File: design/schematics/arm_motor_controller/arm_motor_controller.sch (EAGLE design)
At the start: 59 parts, among them Q1 PFET-FQP27P06, Q2 PFET-FQP27P06, Q3 NFET-FQP30N06L, Q4 NFET-FQP30N06L, Q5 PFET-FQP27P06, Q6 PFET-FQP27P06, Q7 NFET-FQP30N06L, Q8 NFET-FQP30N06L, U1 V_REG_LD1085D2

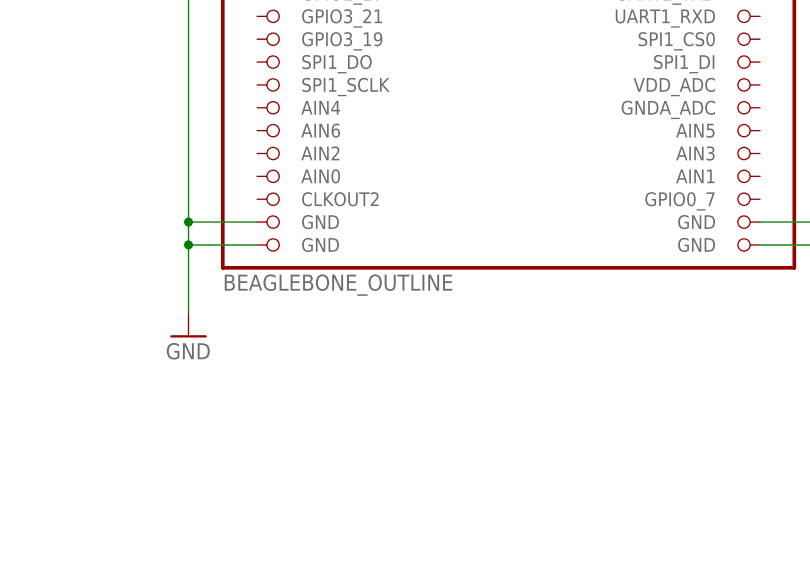
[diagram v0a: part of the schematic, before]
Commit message: updated adafruit library
to have a version of the board which only shows the outline, but doesn't
set the dimension layer.  also added the adafruit library to the repo
for use with other schematics.
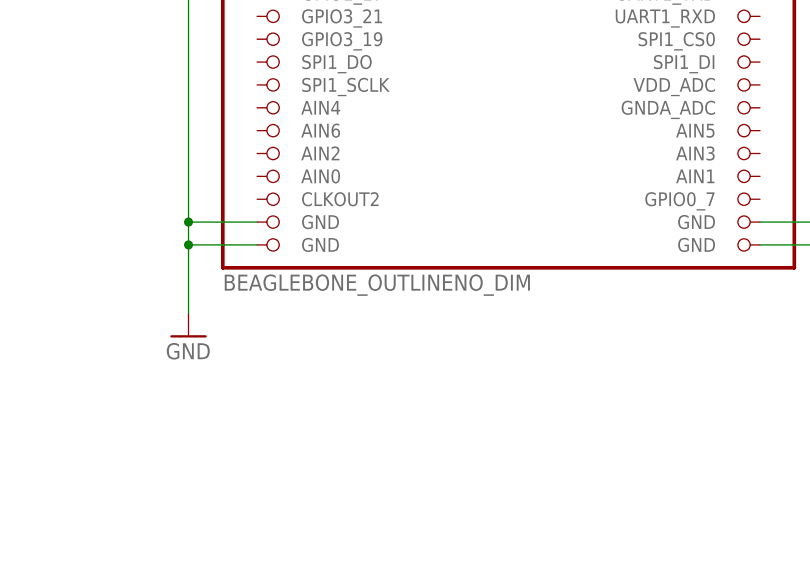
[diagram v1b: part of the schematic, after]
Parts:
- U$1: value BEAGLEBONE_OUTLINE -> BEAGLEBONE_OUTLINENO_DIM; device adafruit:BEAGLEBONE_OUTLINE -> adafruit:BEAGLEBONE_OUTLINENO_DIM
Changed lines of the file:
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@@
 <grid distance="0.1" unitdist="inch" unit="inch" style="lines" multiple="1" display="no" altdistance="0.01" altunitdist="inch" altunit="inch"/>
 <layers>
-<layer number="1" name="Top" color="4" fill="1" visible="no" active="no"/>
-<layer number="2" name="Route2" color="1" fill="3" visible="no" active="no"/>
-<layer number="3" name="Route3" color="4" fill="3" visible="no" active="no"/>
-<layer number="14" name="Route14" color="1" fill="6" visible="no" active="no"/>
-<layer number="15" name="Route15" color="4" fill="6" visible="no" active="no"/>
-<layer number="16" name="Bottom" color="1" fill="1" visible="no" active="no"/>
-<layer number="17" name="Pads" color="2" fill="1" visible="no" active="no"/>
-<layer number="18" name="Vias" color="2" fill="1" visible="no" active="no"/>
-<layer number="19" name="Unrouted" color="6" fill="1" visible="no" active="no"/>
-<layer number="20" name="Dimension" color="15" fill="1" visible="no" active="no"/>
-<layer number="21" name="tPlace" color="7" fill="1" visible="no" active="no"/>
-<layer number="22" name="bPlace" color="7" fill="1" visible="no" active="no"/>
-<layer number="23" name="tOrigins" color="15" fill="1" visible="no" active="no"/>
-<layer number="24" name="bOrigins" color="15" fill="1" visible="no" active="no"/>
-<layer number="25" name="tNames" color="7" fill="1" visible="no" active="no"/>
-<layer number="26" name="bNames" color="7" fill="1" visible="no" active="no"/>
-<layer number="27" name="tValues" color="7" fill="1" visible="no" active="no"/>
-<layer number="28" name="bValues" color="7" fill="1" visible="no" active="no"/>
+<layer number="1" name="Top" color="4" fill="1" visible="yes" active="no"/>
+<layer number="2" name="Route2" color="1" fill="3" visible="yes" active="no"/>
+<layer number="3" name="Route3" color="4" fill="3" visible="yes" active="no"/>
+<layer number="14" name="Route14" color="1" fill="6" visible="yes" active="no"/>
+<layer number="15" name="Route15" color="4" fill="6" visible="yes" active="no"/>
+<layer number="16" name="Bottom" color="1" fill="1" visible="yes" active="no"/>
+<layer number="17" name="Pads" color="2" fill="1" visible="yes" active="no"/>
+<layer number="18" name="Vias" color="2" fill="1" visible="yes" active="no"/>
+<layer number="19" name="Unrouted" color="6" fill="1" visible="yes" active="no"/>
+<layer number="20" name="Dimension" color="15" fill="1" visible="yes" active="no"/>
+<layer number="21" name="tPlace" color="7" fill="1" visible="yes" active="no"/>
+<layer number="22" name="bPlace" color="7" fill="1" visible="yes" active="no"/>
+<layer number="23" name="tOrigins" color="15" fill="1" visible="yes" active="no"/>
+<layer number="24" name="bOrigins" color="15" fill="1" visible="yes" active="no"/>
+<layer number="25" name="tNames" color="7" fill="1" visible="yes" active="no"/>
+<layer number="26" name="bNames" color="7" fill="1" visible="yes" active="no"/>
+<layer number="27" name="tValues" color="7" fill="1" visible="yes" active="no"/>
+<layer number="28" name="bValues" color="7" fill="1" visible="yes" active="no"/>
 <layer number="29" name="tStop" color="7" fill="3" visible="no" active="no"/>
 <layer number="30" name="bStop" color="7" fill="6" visible="no" active="no"/>
@@
 <layer number="35" name="tGlue" color="7" fill="4" visible="no" active="no"/>
 <layer number="36" name="bGlue" color="7" fill="5" visible="no" active="no"/>
-<layer number="37" name="tTest" color="7" fill="1" visible="no" active="no"/>
-<layer number="38" name="bTest" color="7" fill="1" visible="no" active="no"/>
+<layer number="37" name="tTest" color="7" fill="1" visible="yes" active="no"/>
+<layer number="38" name="bTest" color="7" fill="1" visible="yes" active="no"/>
 <layer number="39" name="tKeepout" color="4" fill="11" visible="no" active="no"/>
 <layer number="40" name="bKeepout" color="1" fill="11" visible="no" active="no"/>
@@
 <layer number="44" name="Drills" color="7" fill="1" visible="no" active="no"/>
 <layer number="45" name="Holes" color="7" fill="1" visible="no" active="no"/>
-<layer number="46" name="Milling" color="3" fill="1" visible="no" active="no"/>
-<layer number="47" name="Measures" color="7" fill="1" visible="no" active="no"/>
-<layer number="48" name="Document" color="7" fill="1" visible="no" active="no"/>
-<layer number="49" name="Reference" color="7" fill="1" visible="no" active="no"/>
-<layer number="50" name="dxf" color="7" fill="1" visible="no" active="no"/>
-<layer number="51" name="tDocu" color="7" fill="1" visible="no" active="no"/>
-<layer number="52" name="bDocu" color="7" fill="1" visible="no" active="no"/>
-<layer number="53" name="tGND_GNDA" color="7" fill="9" visible="no" active="no"/>
-<layer number="54" name="bGND_GNDA" color="1" fill="9" visible="no" active="no"/>
-<layer number="56" name="wert" color="7" fill="1" visible="no" active="no"/>
-<layer number="57" name="tCAD" color="7" fill="1" visible="no" active="no"/>
+<layer number="46" name="Milling" color="3" fill="1" visible="yes" active="no"/>
+<layer number="47" name="Measures" color="7" fill="1" visible="yes" active="no"/>
+<layer number="48" name="Document" color="7" fill="1" visible="yes" active="no"/>
+<layer number="49" name="Reference" color="7" fill="1" visible="yes" active="no"/>
+<layer number="50" name="dxf" color="7" fill="1" visible="yes" active="no"/>
+<layer number="51" name="tDocu" color="7" fill="1" visible="yes" active="no"/>
+<layer number="52" name="bDocu" color="7" fill="1" visible="yes" active="no"/>
+<layer number="53" name="tGND_GNDA" color="7" fill="9" visible="yes" active="no"/>
+<layer number="54" name="bGND_GNDA" color="1" fill="9" visible="yes" active="no"/>
+<layer number="56" name="wert" color="7" fill="1" visible="yes" active="no"/>
+<layer number="57" name="tCAD" color="7" fill="1" visible="yes" active="no"/>
+<layer number="59" name="tCarbon" color="7" fill="1" visible="yes" active="no"/>
+<layer number="60" name="bCarbon" color="7" fill="1" visible="yes" active="no"/>
 <layer number="90" name="Modules" color="5" fill="1" visible="yes" active="yes"/>
 <layer number="91" name="Nets" color="2" fill="1" visible="yes" active="yes"/>
@@
 <layer number="113" name="IDFDebug" color="4" fill="1" visible="yes" active="yes"/>
 <layer number="116" name="Patch_BOT" color="9" fill="4" visible="yes" active="yes"/>
+<layer number="118" name="Rect_Pads" color="7" fill="1" visible="no" active="no"/>
 <layer number="121" name="_tsilk" color="7" fill="1" visible="yes" active="yes"/>
 <layer number="122" name="_bsilk" color="7" fill="1" visible="yes" active="yes"/>
@@
 <layer number="127" name="_tValues" color="7" fill="1" visible="yes" active="yes"/>
 <layer number="128" name="_bValues" color="7" fill="1" visible="yes" active="yes"/>
+<layer number="129" name="Mask" color="7" fill="1" visible="yes" active="yes"/>
 <layer number="131" name="tAdjust" color="7" fill="1" visible="no" active="yes"/>
 <layer number="132" name="bAdjust" color="7" fill="1" visible="no" active="yes"/>
@@
 <layer number="230" name="230bmp" color="7" fill="1" visible="yes" active="yes"/>
 <layer number="231" name="231bmp" color="7" fill="1" visible="yes" active="yes"/>
+<layer number="232" name="Eagle3D_PG2" color="7" fill="1" visible="no" active="no"/>
+<layer number="233" name="Eagle3D_PG3" color="7" fill="1" visible="no" active="no"/>
 <layer number="248" name="Housing" color="7" fill="1" visible="yes" active="yes"/>
 <layer number="249" name="Edge" color="7" fill="1" visible="yes" active="yes"/>
@@
 </classes>
 <parts>
-<part name="U$1" library="adafruit" deviceset="BEAGLEBONE_OUTLINE" device=""/>
+<part name="U$1" library="adafruit" deviceset="BEAGLEBONE_OUTLINE" device="NO_DIM" value="BEAGLEBONE_OUTLINENO_DIM"/>
 <part name="U1" library="SparkFun-PowerIC" deviceset="V_REG_LD1085" device="D2">
 <attribute name="MANEX" value="140-0004281"/>

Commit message: working on schematic/board.
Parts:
- removed R1: 370, SparkFun-Passives:RESISTOR0402-RES
- removed R2: 1.5k, SparkFun-Passives:RESISTOR0402-RES
- removed U1: V_REG_LD1085D2, SparkFun-PowerIC:V_REG_LD1085D2
- added +HLS, +RLS, -HLS, -RLS: M02POLAR, SparkFun-Connectors:M02POLAR
- added D7: (no value), SparkFun-LED:LED-FKIT-1206
- added LD1085: V_REG_317SINK, SparkFun-PowerIC:V_REG_317SINK
- added R28: 50, resistor:R-EU_M0805
- added SERVO1: AX-12A, molex-spox:AX-12A
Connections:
- removed net N$16: R11.2, T4.B
- removed net N$4: R1.1, R2.2, U1.ADJ
- new net +HEIGHT_LS: +HLS.2, R7.2, T2.B, U$1.GPIO2_9
- new net +RADIUS_LS: +RLS.2, R11.2, T4.B, U$1.GPIO2_8
- new net -HEIGHT_LS: -HLS.2, R6.1, T1.B, U$1.GPIO2_11
- new net -RADIUS_LS: -RLS.2, R10.1, T3.B, U$1.GPIO2_10
- new net N$19: U$1.GPIO2_7
- net 12V: now also SERVO1.VDD
- net BBB_TX: now also D7.A
- net GND: now also +HLS.1, +RLS.1, -HLS.1, -RLS.1, LD1085.ADJ, R28.1, SERVO1.GND; no longer R2.1
- net N$10: now also U$1.GPIO2_6; no longer R7.2, T2.B
- net N$15: now also U$1.GPIO0_26; no longer R10.1, T3.B
- net N$3: now also LD1085.IN; no longer U1.IN
- net N$9: now also D7.C, R28.2; no longer R6.1, T1.B
- net SERVO_TX/RX: now also SERVO1.DATA
- net VOUT: now also LD1085.OUT; no longer R1.2, U1.OUT, U1.OUT@1
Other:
- note added: "B"
- note added: "Encoder Feedback:"
- note added: "LED Display:"
- note added: "Limit Switches:"
- note added: "Motor Drivers:"
- note added: "Power Regulation:"
- note added: "Servo Serial Buffer:"
- note removed: "A"
- moved on the sheet: C1, C2, C3, D1, D2, D3, D4, D5, D6, JP1, Q1, Q2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

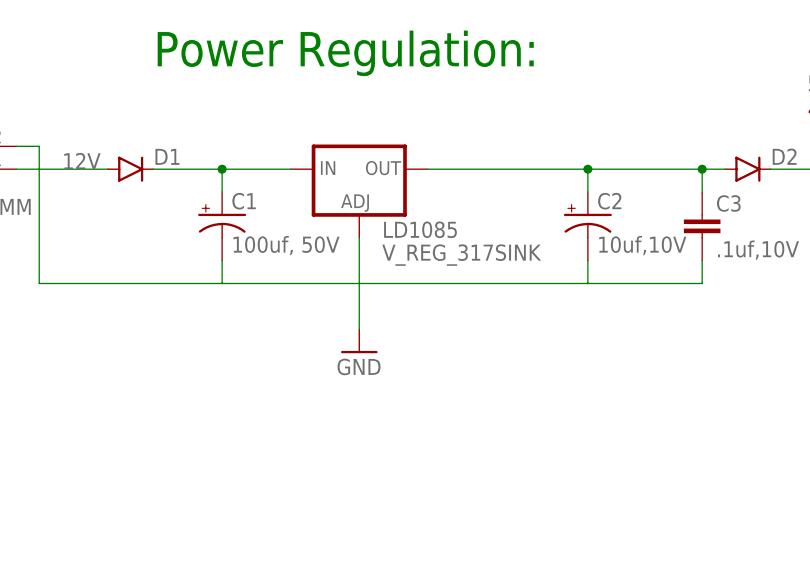
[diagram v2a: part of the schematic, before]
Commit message: routed the board.
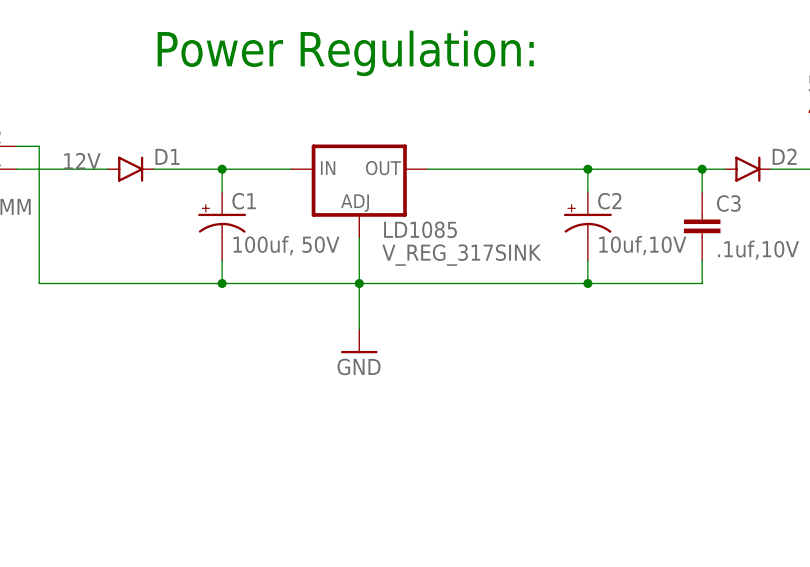
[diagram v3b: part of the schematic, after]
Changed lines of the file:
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@@
 <?xml version="1.0" encoding="utf-8"?>
 <!DOCTYPE eagle SYSTEM "eagle.dtd">
-<eagle version="7.2.0">
+<eagle version="7.5.0">
 <drawing>
 <settings>
@@
 <grid distance="0.1" unitdist="inch" unit="inch" style="lines" multiple="1" display="no" altdistance="0.01" altunitdist="inch" altunit="inch"/>
 <layers>
-<layer number="1" name="Top" color="4" fill="1" visible="yes" active="no"/>
-<layer number="2" name="Route2" color="1" fill="3" visible="yes" active="no"/>
-<layer number="3" name="Route3" color="4" fill="3" visible="yes" active="no"/>
-<layer number="14" name="Route14" color="1" fill="6" visible="yes" active="no"/>
-<layer number="15" name="Route15" color="4" fill="6" visible="yes" active="no"/>
-<layer number="16" name="Bottom" color="1" fill="1" visible="yes" active="no"/>
-<layer number="17" name="Pads" color="2" fill="1" visible="yes" active="no"/>
-<layer number="18" name="Vias" color="2" fill="1" visible="yes" active="no"/>
-<layer number="19" name="Unrouted" color="6" fill="1" visible="yes" active="no"/>
-<layer number="20" name="Dimension" color="15" fill="1" visible="yes" active="no"/>
-<layer number="21" name="tPlace" color="7" fill="1" visible="yes" active="no"/>
-<layer number="22" name="bPlace" color="7" fill="1" visible="yes" active="no"/>
-<layer number="23" name="tOrigins" color="15" fill="1" visible="yes" active="no"/>
-<layer number="24" name="bOrigins" color="15" fill="1" visible="yes" active="no"/>
-<layer number="25" name="tNames" color="7" fill="1" visible="yes" active="no"/>
-<layer number="26" name="bNames" color="7" fill="1" visible="yes" active="no"/>
-<layer number="27" name="tValues" color="7" fill="1" visible="yes" active="no"/>
-<layer number="28" name="bValues" color="7" fill="1" visible="yes" active="no"/>
+<layer number="1" name="Top" color="4" fill="1" visible="no" active="no"/>
+<layer number="2" name="Route2" color="1" fill="3" visible="no" active="no"/>
+<layer number="3" name="Route3" color="4" fill="3" visible="no" active="no"/>
+<layer number="14" name="Route14" color="1" fill="6" visible="no" active="no"/>
+<layer number="15" name="Route15" color="4" fill="6" visible="no" active="no"/>
+<layer number="16" name="Bottom" color="1" fill="1" visible="no" active="no"/>
+<layer number="17" name="Pads" color="2" fill="1" visible="no" active="no"/>
+<layer number="18" name="Vias" color="2" fill="1" visible="no" active="no"/>
+<layer number="19" name="Unrouted" color="6" fill="1" visible="no" active="no"/>
+<layer number="20" name="Dimension" color="15" fill="1" visible="no" active="no"/>
+<layer number="21" name="tPlace" color="7" fill="1" visible="no" active="no"/>
+<layer number="22" name="bPlace" color="7" fill="1" visible="no" active="no"/>
+<layer number="23" name="tOrigins" color="15" fill="1" visible="no" active="no"/>
+<layer number="24" name="bOrigins" color="15" fill="1" visible="no" active="no"/>
+<layer number="25" name="tNames" color="7" fill="1" visible="no" active="no"/>
+<layer number="26" name="bNames" color="7" fill="1" visible="no" active="no"/>
+<layer number="27" name="tValues" color="7" fill="1" visible="no" active="no"/>
+<layer number="28" name="bValues" color="7" fill="1" visible="no" active="no"/>
 <layer number="29" name="tStop" color="7" fill="3" visible="no" active="no"/>
 <layer number="30" name="bStop" color="7" fill="6" visible="no" active="no"/>
@@
 <layer number="35" name="tGlue" color="7" fill="4" visible="no" active="no"/>
 <layer number="36" name="bGlue" color="7" fill="5" visible="no" active="no"/>
-<layer number="37" name="tTest" color="7" fill="1" visible="yes" active="no"/>
-<layer number="38" name="bTest" color="7" fill="1" visible="yes" active="no"/>
+<layer number="37" name="tTest" color="7" fill="1" visible="no" active="no"/>
+<layer number="38" name="bTest" color="7" fill="1" visible="no" active="no"/>
 <layer number="39" name="tKeepout" color="4" fill="11" visible="no" active="no"/>
 <layer number="40" name="bKeepout" color="1" fill="11" visible="no" active="no"/>
@@
 <layer number="44" name="Drills" color="7" fill="1" visible="no" active="no"/>
 <layer number="45" name="Holes" color="7" fill="1" visible="no" active="no"/>
-<layer number="46" name="Milling" color="3" fill="1" visible="yes" active="no"/>
-<layer number="47" name="Measures" color="7" fill="1" visible="yes" active="no"/>
-<layer number="48" name="Document" color="7" fill="1" visible="yes" active="no"/>
-<layer number="49" name="Reference" color="7" fill="1" visible="yes" active="no"/>
-<layer number="50" name="dxf" color="7" fill="1" visible="yes" active="no"/>
-<layer number="51" name="tDocu" color="7" fill="1" visible="yes" active="no"/>
-<layer number="52" name="bDocu" color="7" fill="1" visible="yes" active="no"/>
-<layer number="53" name="tGND_GNDA" color="7" fill="9" visible="yes" active="no"/>
-<layer number="54" name="bGND_GNDA" color="1" fill="9" visible="yes" active="no"/>
-<layer number="56" name="wert" color="7" fill="1" visible="yes" active="no"/>
-<layer number="57" name="tCAD" color="7" fill="1" visible="yes" active="no"/>
-<layer number="59" name="tCarbon" color="7" fill="1" visible="yes" active="no"/>
-<layer number="60" name="bCarbon" color="7" fill="1" visible="yes" active="no"/>
+<layer number="46" name="Milling" color="3" fill="1" visible="no" active="no"/>
+<layer number="47" name="Measures" color="7" fill="1" visible="no" active="no"/>
+<layer number="48" name="Document" color="7" fill="1" visible="no" active="no"/>
+<layer number="49" name="Reference" color="7" fill="1" visible="no" active="no"/>
+<layer number="50" name="dxf" color="7" fill="1" visible="no" active="no"/>
+<layer number="51" name="tDocu" color="7" fill="1" visible="no" active="no"/>
+<layer number="52" name="bDocu" color="7" fill="1" visible="no" active="no"/>
+<layer number="53" name="tGND_GNDA" color="7" fill="9" visible="no" active="no"/>
+<layer number="54" name="bGND_GNDA" color="1" fill="9" visible="no" active="no"/>
+<layer number="56" name="wert" color="7" fill="1" visible="no" active="no"/>
+<layer number="57" name="tCAD" color="7" fill="1" visible="no" active="no"/>
+<layer number="59" name="tCarbon" color="7" fill="1" visible="no" active="no"/>
+<layer number="60" name="bCarbon" color="7" fill="1" visible="no" active="no"/>
 <layer number="90" name="Modules" color="5" fill="1" visible="yes" active="yes"/>
 <layer number="91" name="Nets" color="2" fill="1" visible="yes" active="yes"/>
@@
 <wire x1="-48.26" y1="33.02" x2="-48.26" y2="17.78" width="0.1524" layer="91"/>
 <wire x1="-48.26" y1="17.78" x2="-27.94" y2="17.78" width="0.1524" layer="91"/>
+<junction x="-27.94" y="17.78"/>
+<junction x="-12.7" y="17.78"/>
+<junction x="12.7" y="17.78"/>
 </segment>
 </net>

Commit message: finalizing motor control board.
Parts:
- renumbered Q1 to PFET01, Q2 to PFET02, Q3 to NFET01, Q4 to NFET02, Q5 to PFET03, Q6 to PFET04, Q7 to NFET03, Q8 to NFET04
